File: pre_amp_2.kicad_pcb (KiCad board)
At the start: 2 copper layers, 47.9 x 52.1 mm, 45 parts, among them J1 IN, J10 SW2_3, J11 SW2_1, J12 SW2_4, J13 VR5_3, J14 VR5_1, J15 OUT, J2 GND2, J3 Vin, J4 GND, J5 VR1_1, J6 VR3_3, J7 VR1_3, J9 VR4_2, U1 TL072, U2 ICL7660

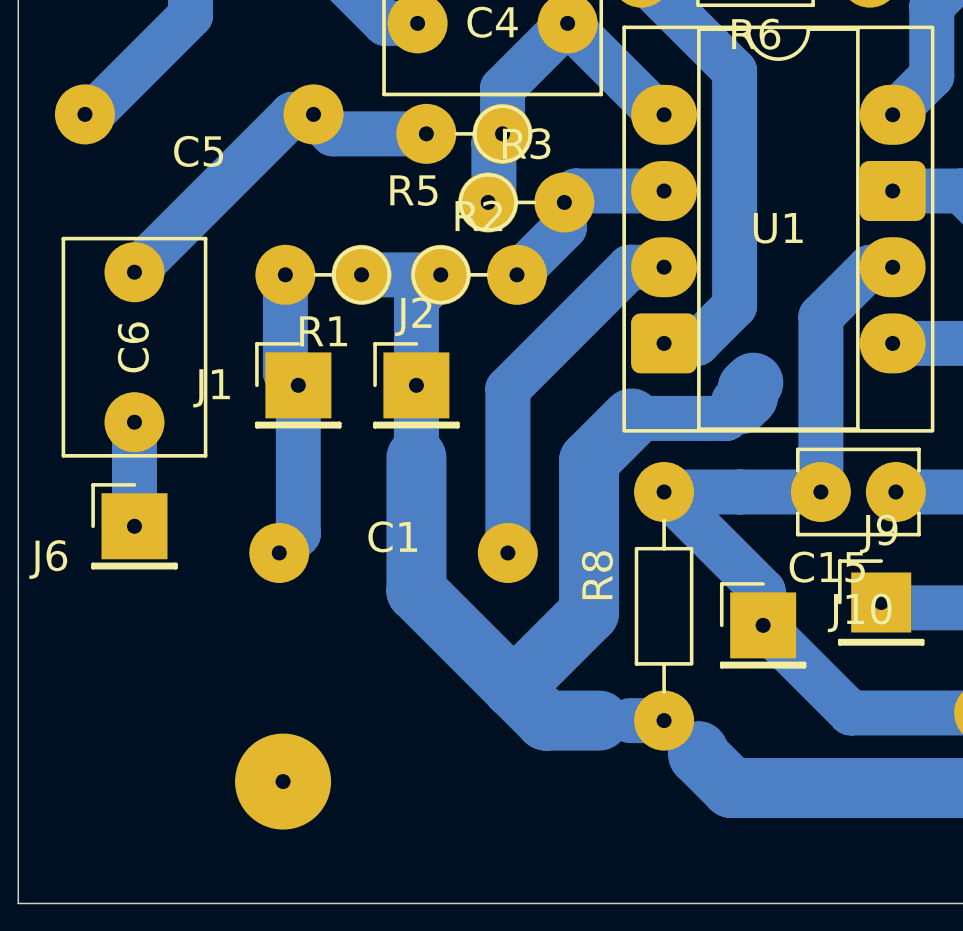
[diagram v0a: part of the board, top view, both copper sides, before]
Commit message: 入力部分が抵抗(GND)->コンデンサ->ICだったのをコンデンサ->抵抗(GND)->ICに変更。 (直流がICにたまってGNDに落ちず音が出なくなる)
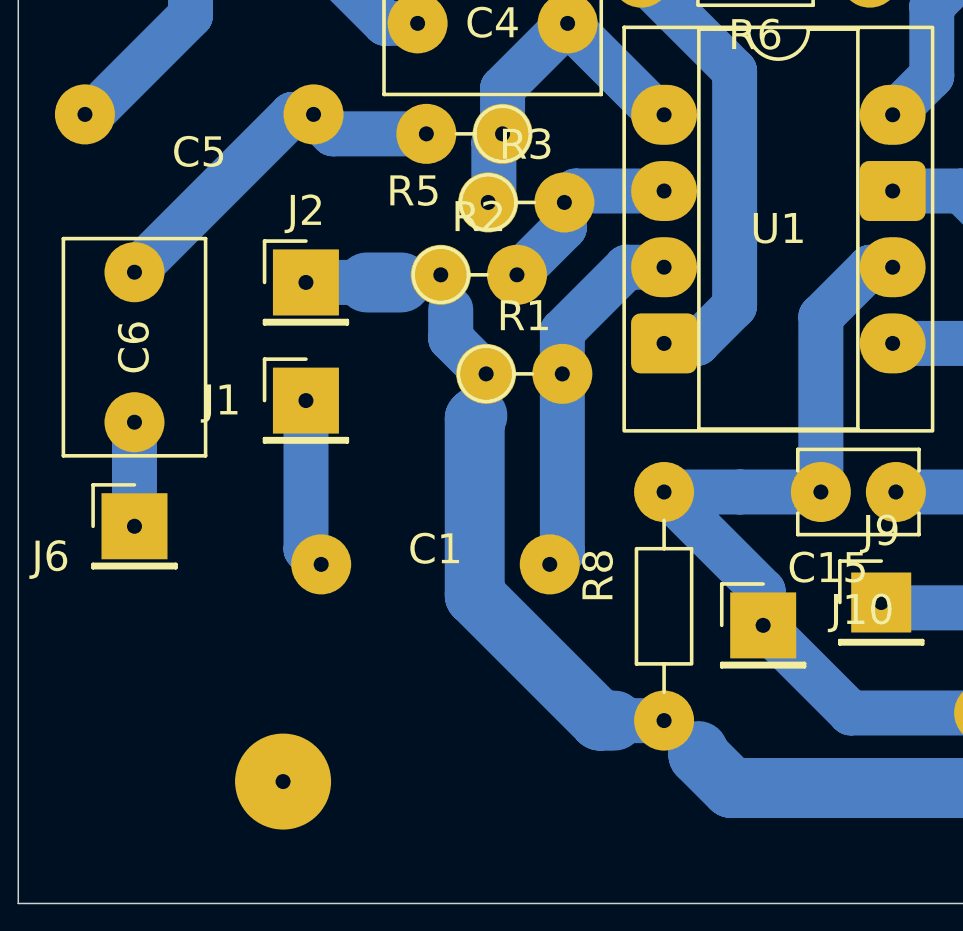
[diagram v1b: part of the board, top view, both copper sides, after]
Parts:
- moved R1 5.30 mm to (134.8, 79.8), turned to 0 degrees
- moved J2 5.03 mm to (128.8, 76.7)
- moved C1 1.45 mm to (133.1, 86.1)
- moved J1 0.57 mm to (128.8, 80.6)
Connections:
- R1 pad 2: Net-(J1-Pin_1) -> Net-(U1A-+)
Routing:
- net GND2: track 57.7 -> 40.0 mm
- net Net-(J1-Pin_1): track 9.71 -> 5.67 mm

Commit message: オペアンプのパスコンを基板上に配置しようとしたけど諦めて 裏に繋ぐ
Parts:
- J5: value VR1_1 -> VR3_2

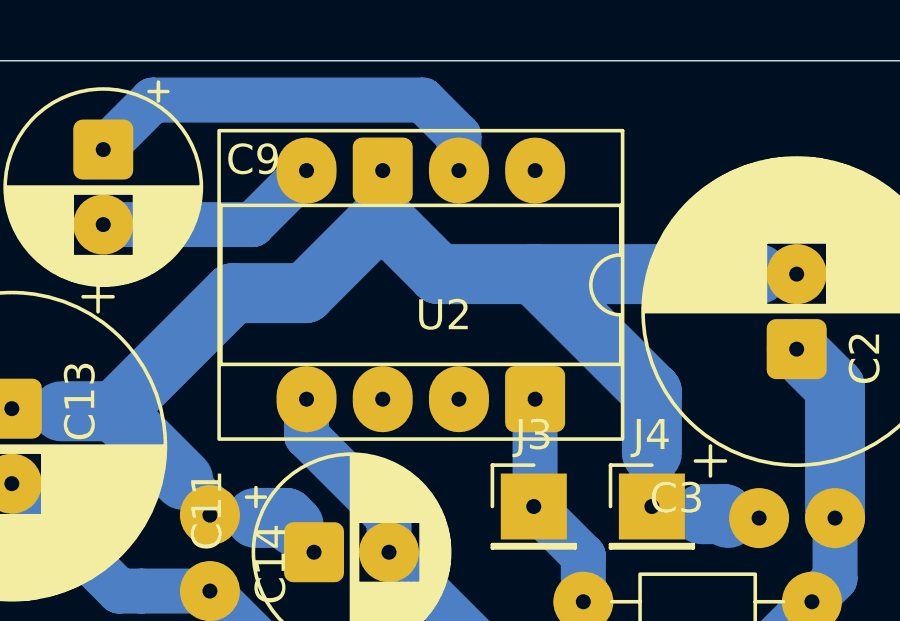
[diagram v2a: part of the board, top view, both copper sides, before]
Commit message: TC1044Sに変更
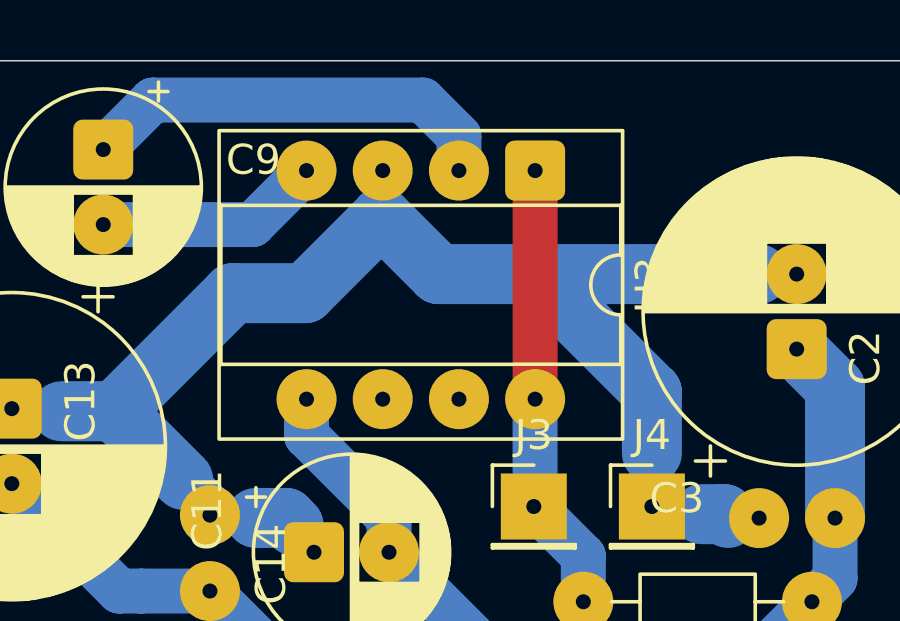
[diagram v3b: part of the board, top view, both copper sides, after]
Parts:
- removed U2: ICL7660, Package_DIP:CERDIP-8_W7.62mm_SideBrazed_Socket
- added U3: TC1044S, Package_DIP:CERDIP-8_W7.62mm_SideBrazed_Socket, F.Cu at (148.0, 49.0)
- R4, R6: value 100 -> 10
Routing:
- net Net-(J3-Pin_1): track 7.46 -> 15.1 mm

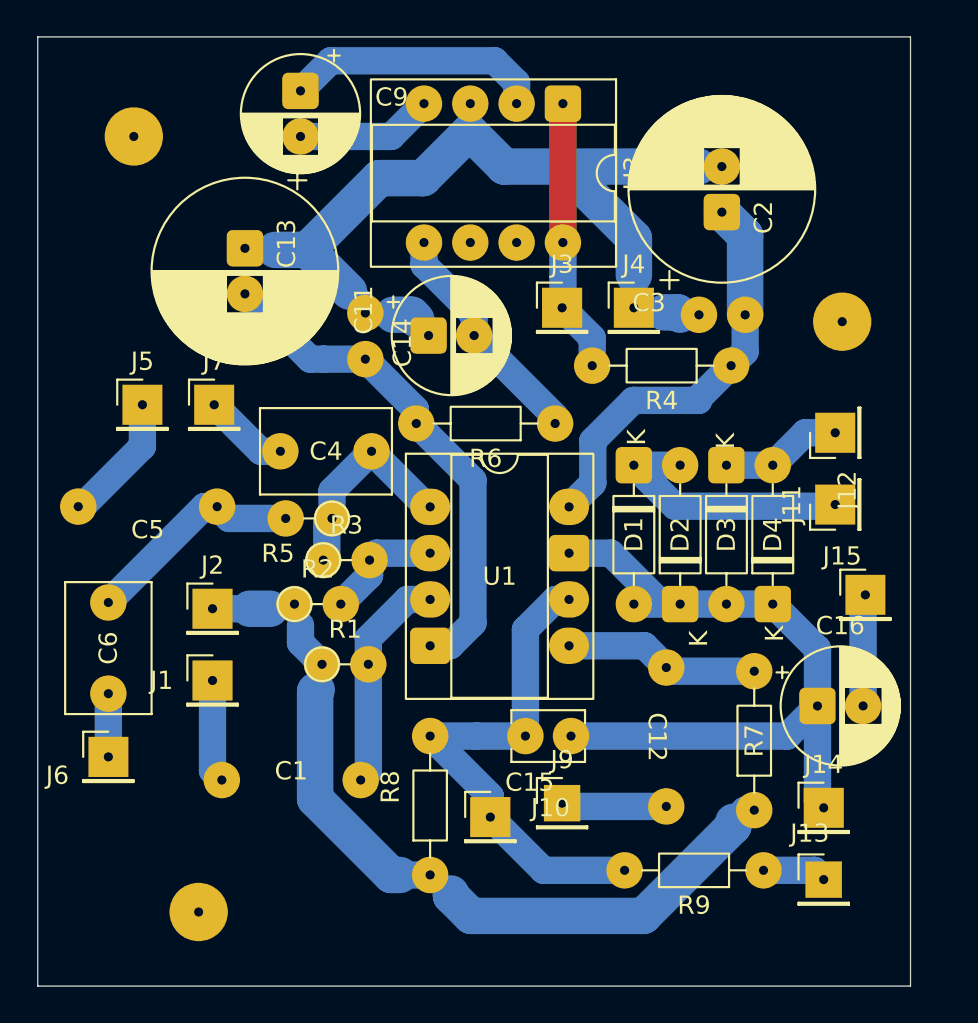
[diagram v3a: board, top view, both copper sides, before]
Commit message: 67番ピンに330pを追加、ICパッケージのすぐ横に付ける
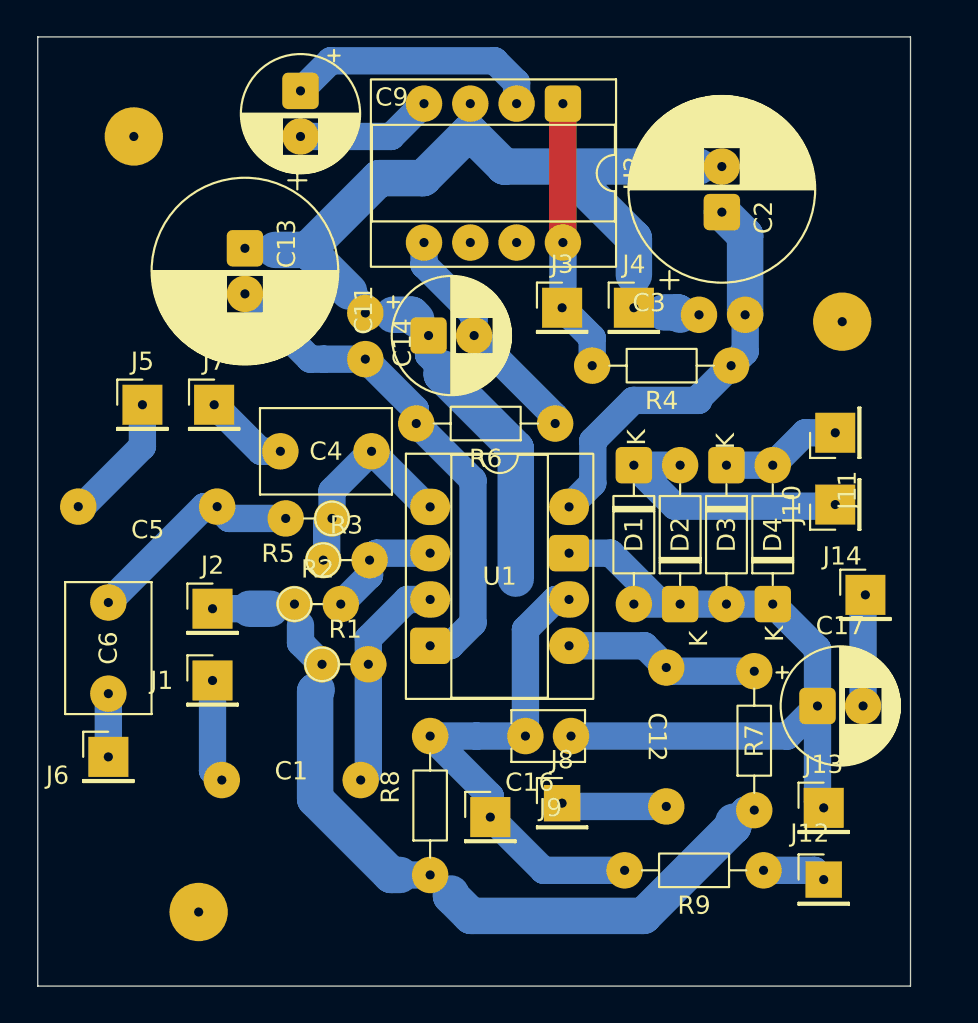
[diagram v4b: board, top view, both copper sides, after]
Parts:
- J5: value VR3_2 -> VR2_2
- renumbered C15 to C16, C16 to C17, J11 to J10, J12 to J11, J13 to J12, J14 to J13, J15 to J14, J9 to J8, J10 to J9, U3 to U2
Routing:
- net GND: track 45.4 -> 60.7 mm

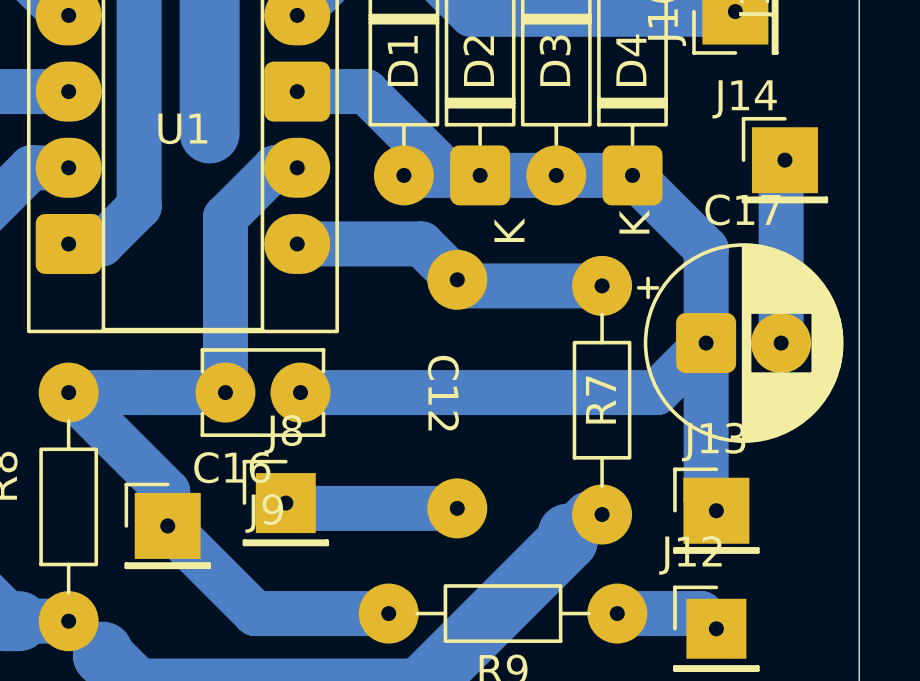
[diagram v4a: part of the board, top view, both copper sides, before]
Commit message: 発振対策で初段の増幅率を上げて後段のボリュームと抵抗の値を調整
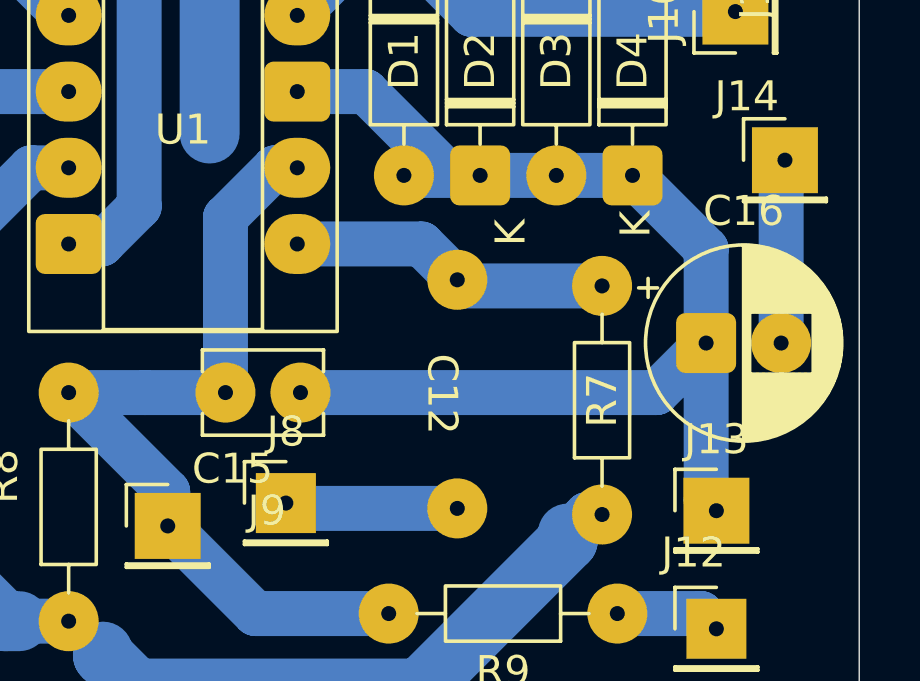
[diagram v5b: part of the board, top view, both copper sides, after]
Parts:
- R3: value 20k -> 39k
- R9: value 10k -> 1k
- renumbered C16 to C15, C17 to C16

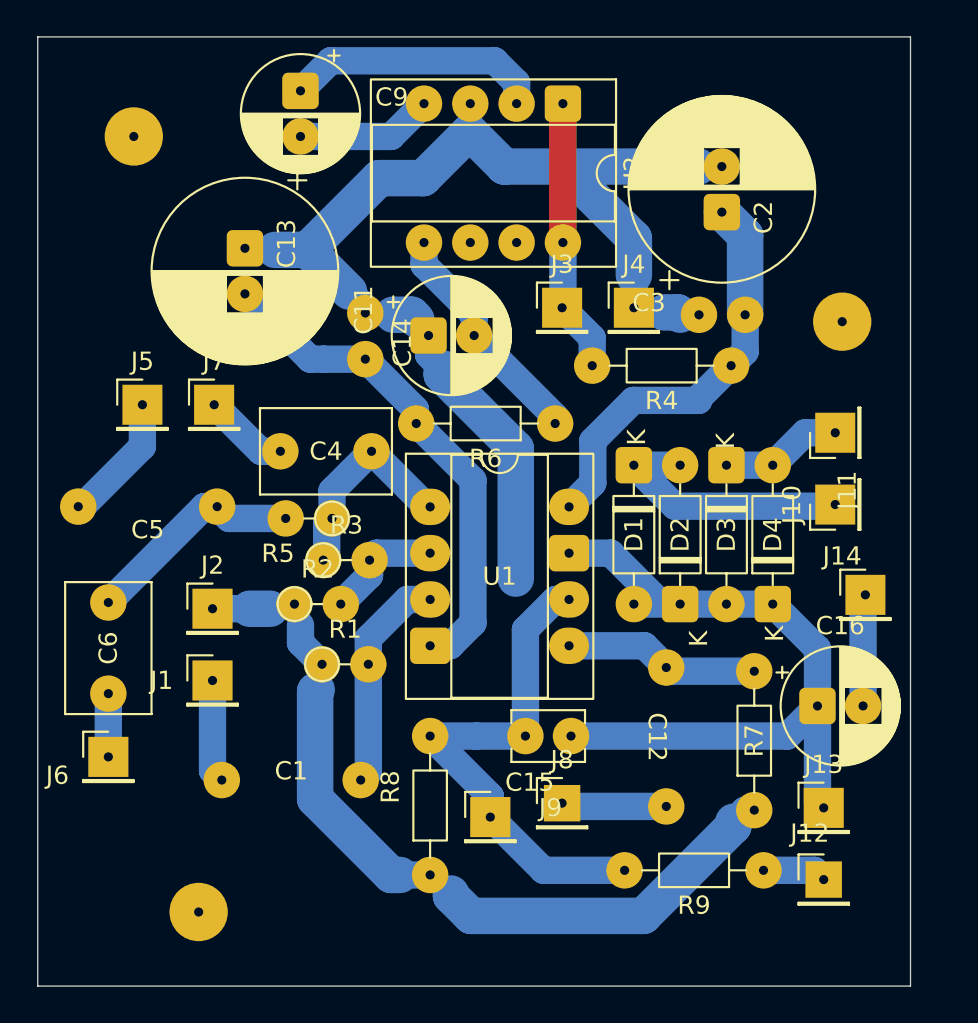
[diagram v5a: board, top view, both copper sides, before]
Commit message: R3を47kに変更、シールド線の網線をGNDに繋ぐ配線を追加。
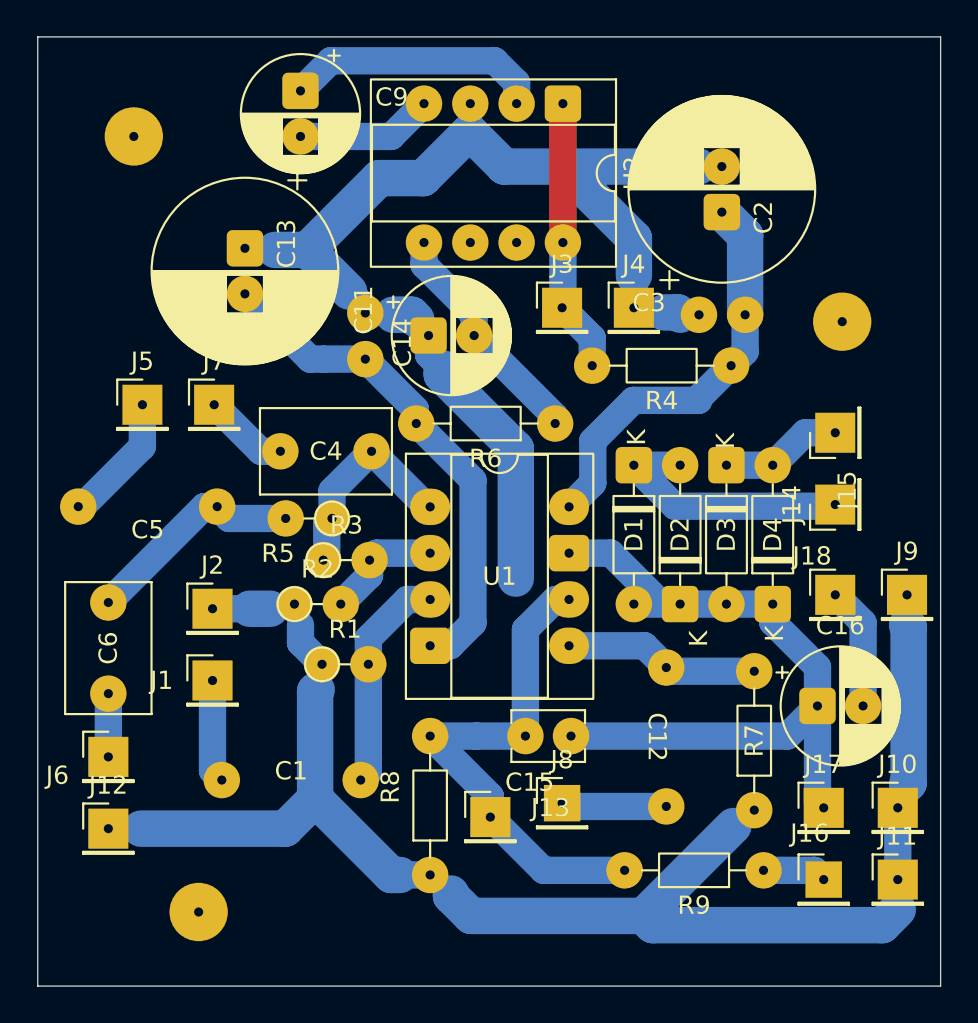
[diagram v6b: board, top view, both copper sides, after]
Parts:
- added J10: GND5_1, Connector_PinHeader_2.54mm:PinHeader_1x01_P2.54mm_Vertical, F.Cu at (166.4, 87.6)
- added J11: GND5_3, Connector_PinHeader_2.54mm:PinHeader_1x01_P2.54mm_Vertical, F.Cu at (166.4, 91.6)
- added J12: GND3_3, Connector_PinHeader_2.54mm:PinHeader_1x01_P2.54mm_Vertical, F.Cu at (123.1, 88.8)
- added J9: GNDOUT, Connector_PinHeader_2.54mm:PinHeader_1x01_P2.54mm_Vertical, F.Cu at (166.9, 75.9)
- R3: value 39k -> 47k
- moved J18 1.65 mm to (162.9, 75.9)
- renumbered J9 to J13, J10 to J14, J11 to J15, J12 to J16, J13 to J17, J14 to J18
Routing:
- net GND2: track 40.0 -> 77.5 mm
- net Net-(J18-Pin_1): track 6.15 -> 6.73 mm
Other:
- board size 47.9 x 52.1 mm -> 49.5 x 52.1 mm

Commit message: チャージポンプの抵抗と電解コンデンサを強化
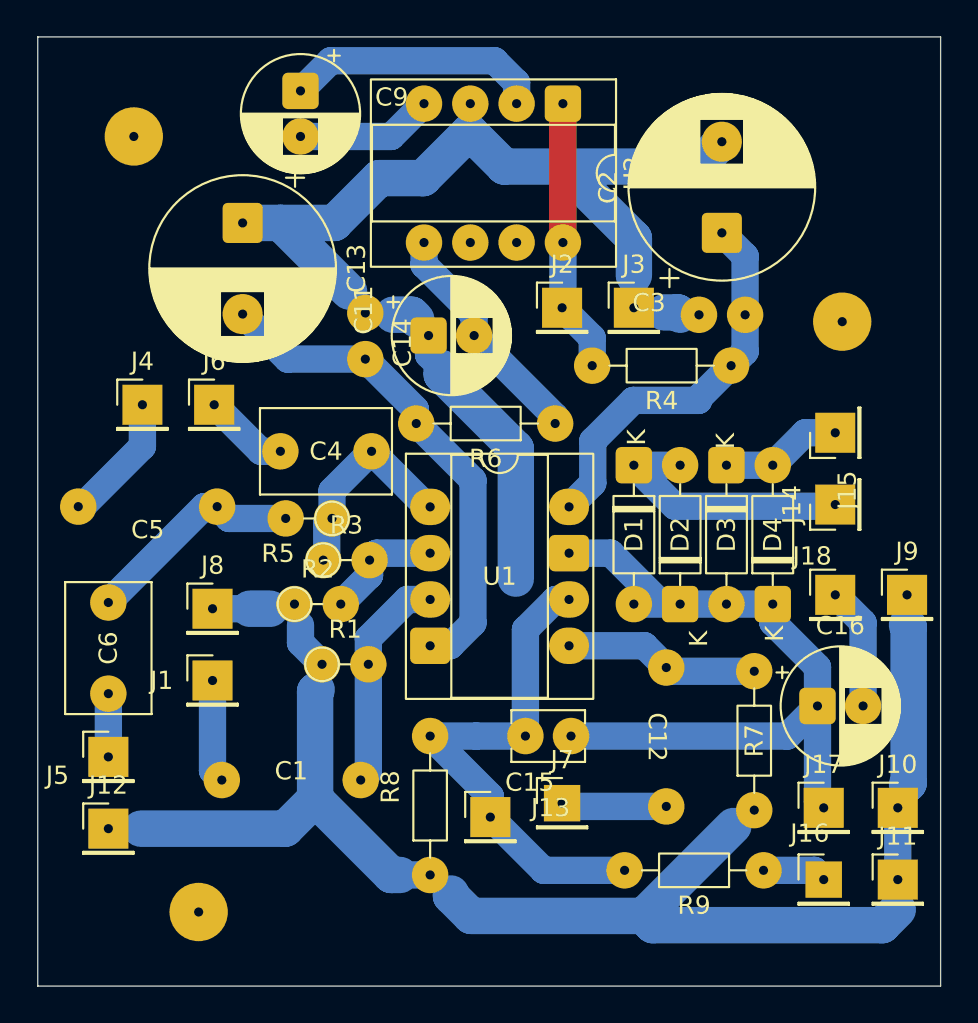
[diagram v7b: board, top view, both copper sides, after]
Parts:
- C13, C2: value 100u -> 1000u; footprint Capacitor_THT:CP_Radial_D10.0mm_P2.50mm -> Capacitor_THT:CP_Radial_D10.0mm_P5.00mm
- J8: renamed from J2; value GND2 -> GNDIN
- R4, R6: value 10 -> 22
- moved C13 1.40 mm to (130.4, 55.5)
- moved C2 1.14 mm to (156.7, 56.1)
- renumbered J3 to J2, J4 to J3, J5 to J4, J6 to J5, J7 to J6, J8 to J7
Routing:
- net GND: track 60.7 -> 64.5 mm
- net Net-(U1C-V+): track 22.8 -> 21.7 mm
